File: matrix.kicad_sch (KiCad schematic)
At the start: 152 parts

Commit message: Flip 2u stabilizers
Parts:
- MX30_2u1, MX50_2u1: footprint Orthgyle:MX_PCB_200B -> Orthgyle:MX_PCB_200H
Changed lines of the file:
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@@
 			)
 		)
-		(property "Footprint" "Orthgyle:MX_PCB_200B"
+		(property "Footprint" "Orthgyle:MX_PCB_200H"
 			(at 162.56 125.73 0)
 			(effects
@@
 			)
 		)
-		(property "Footprint" "Orthgyle:MX_PCB_200B"
+		(property "Footprint" "Orthgyle:MX_PCB_200H"
 			(at 111.76 125.73 0)
 			(effects

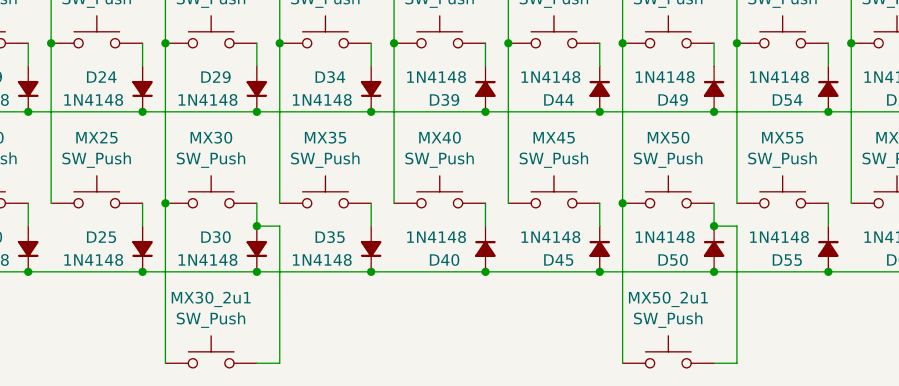
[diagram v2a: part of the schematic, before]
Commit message: Add center offset 2u keys
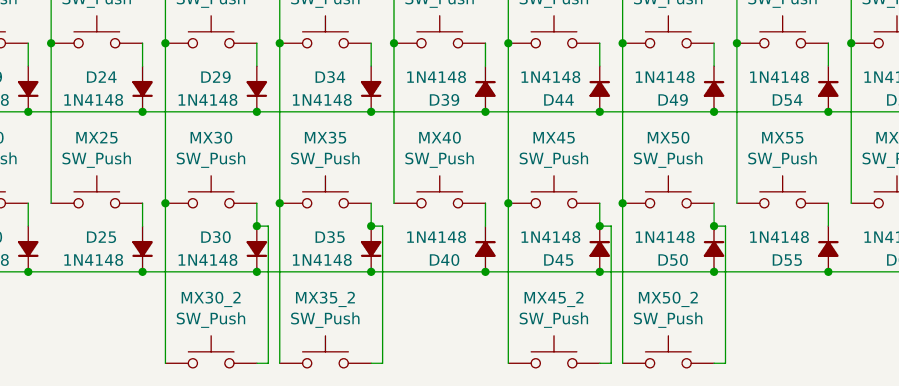
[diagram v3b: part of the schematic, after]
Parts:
- added MX35_2, MX45_2: SW_Push, Orthgyle:MX_PCB_200H, symbol Switch:SW_Push
- renumbered MX30_2u1 to MX30_2, MX50_2u1 to MX50_2
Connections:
- net COL1: now also MX45_2.2
- net COL6: now also MX35_2.2
- net at D35.2 (A), MX35.1: now also MX35_2.1
- net at D45.1 (K), MX45.1: now also MX45_2.1
